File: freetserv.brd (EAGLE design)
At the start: 91.4 x 82.5 mm, 71 parts, among them IC2 SN75240PW, Q1 12MHz, Q2 6MHz, U1 MCP16311-E/MS

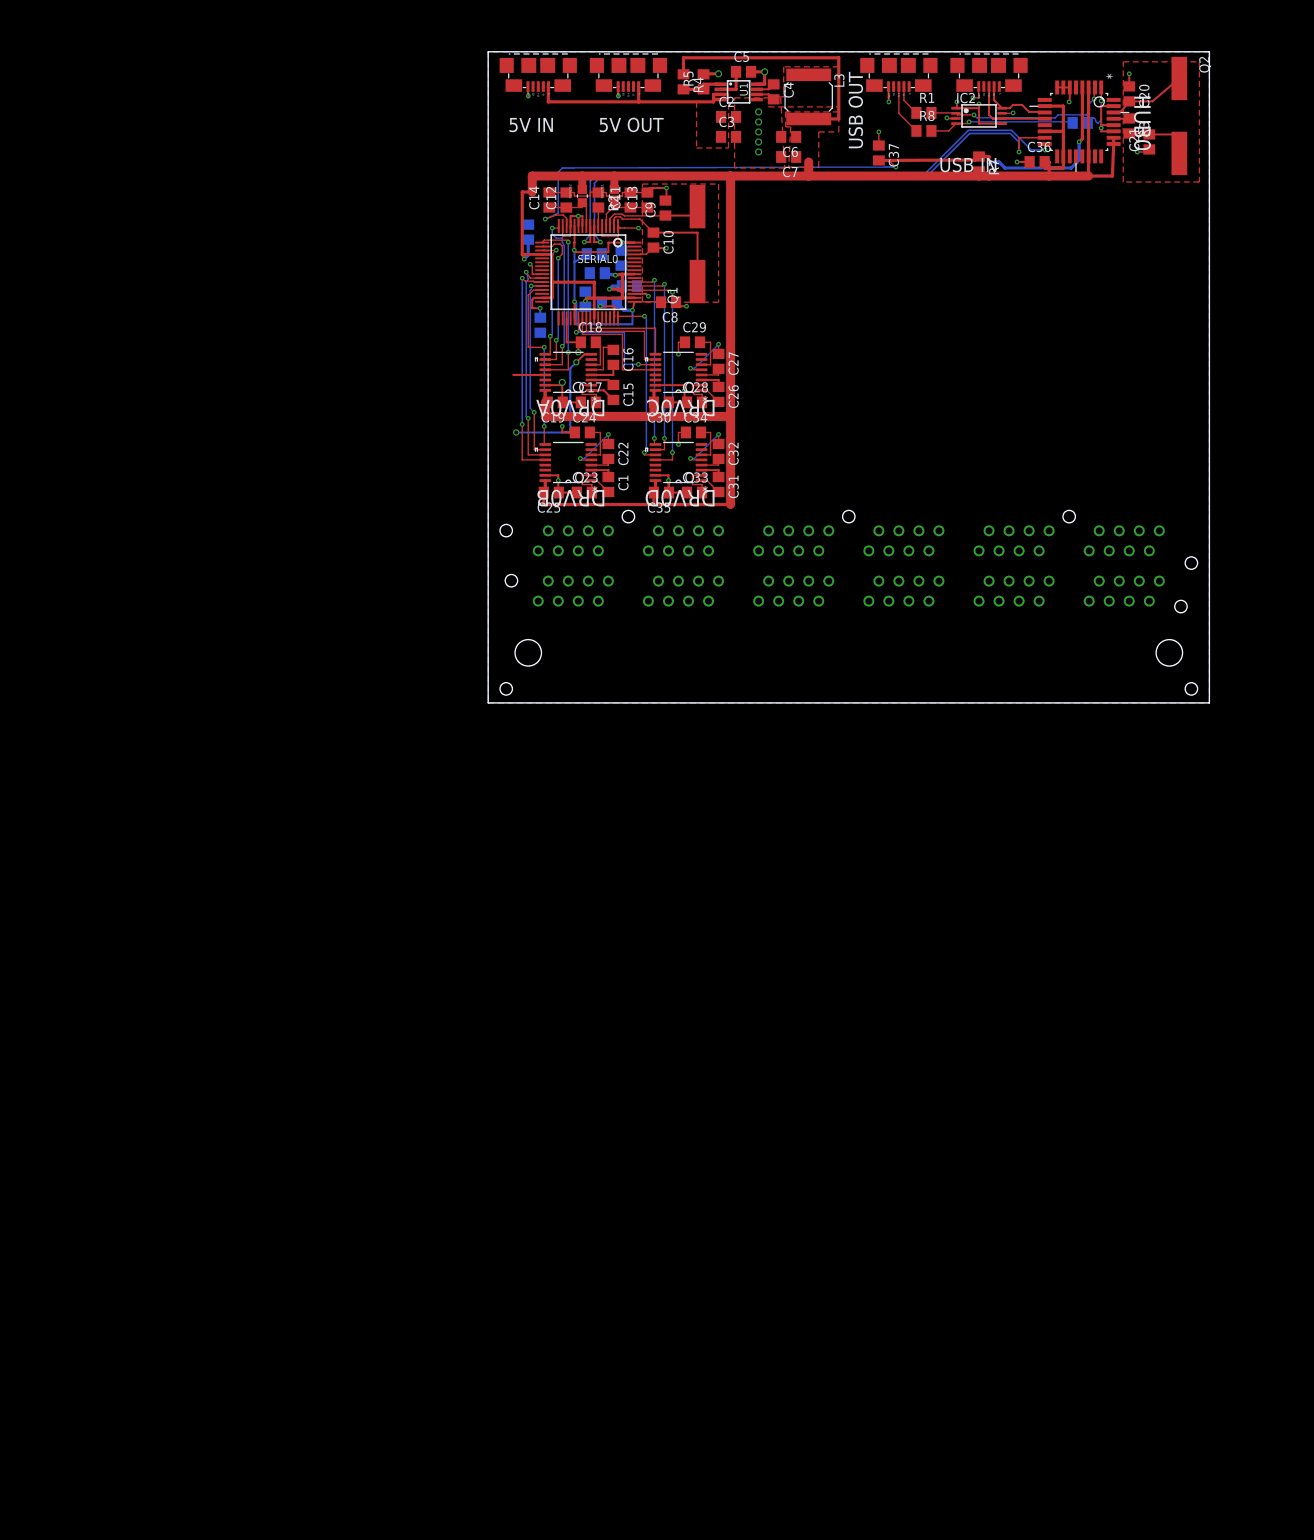
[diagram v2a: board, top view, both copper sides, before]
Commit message: Volker re-organized the schematics
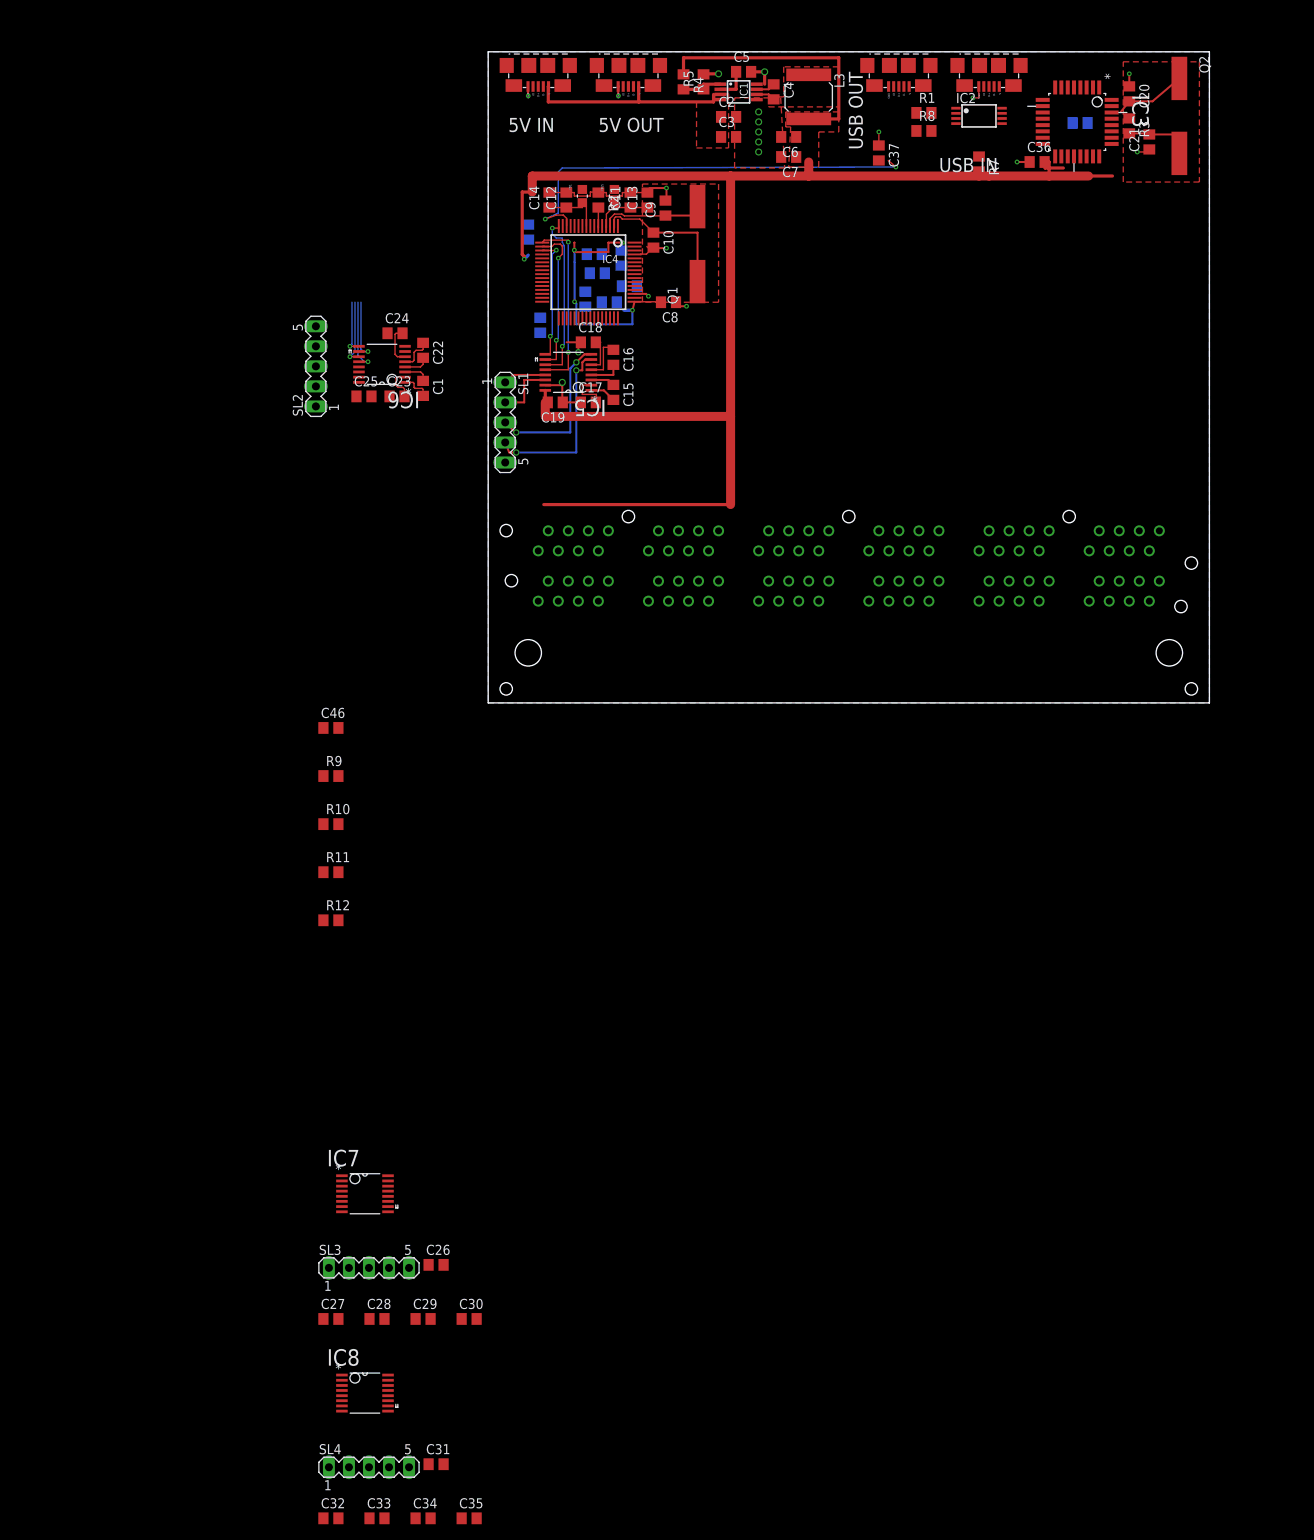
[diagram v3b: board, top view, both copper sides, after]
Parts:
- removed DRV0B, DRV0C, DRV0D: MAX3232ECPW, Texas Instruments_By_element14_Batch_1:SOP65P640X120-16N
- removed HUB0: TUSB2046BVF, Texas Instruments_By_element14_Batch_1:QFP80P900X900X145-32N
- added C46: 0.1uF, resistor:C0805
- added IC3: TUSB2046BVF, Texas Instruments_By_element14_Batch_1:QFP80P900X900X145-32N
- added IC6, IC7, IC8: MAX3232ECPW, Texas Instruments_By_element14_Batch_1:SOP65P640X120-16N
- added R10, R9: 27, resistor:R0805
- added R11, R12: 10k, resistor:R0805
- added SL1, SL2, SL3, SL4: (no value), con-lstb:MA05-1
- R2: value 12K -> 12K / 1%
- moved C32 143.9 mm to (-19.9, -103.4), turned to 0 degrees
- moved C34 141.9 mm to (-8.26, -103.4)
- moved C33 136.1 mm to (-14.1, -103.4)
- moved C35 132.3 mm to (-2.41, -103.4), turned to 0 degrees
- moved C27 131.0 mm to (-19.9, -78.1), turned to 0 degrees
- moved C31 129.3 mm to (-6.60, -96.5), turned to 0 degrees
- moved C29 128.5 mm to (-8.26, -78.1)
- moved C28 123.0 mm to (-14.1, -78.1)
- moved C30 118.7 mm to (-2.41, -78.1), turned to 0 degrees
- moved C26 116.0 mm to (-6.60, -71.2), turned to 0 degrees
- moved C24 26.9 mm to (-11.8, 46.9)
- moved C22 26.8 mm to (-8.26, 44.7)
- moved C23 26.7 mm to (-11.6, 38.9)
- moved C25 26.7 mm to (-15.7, 38.9), turned to 0 degrees
- moved C1 26.5 mm to (-8.26, 39.9)
- renumbered DRV0A to IC5, FERRITE1 to FB2\, FERRITE2 to FB1, SERIAL0 to IC4, U1 to IC1
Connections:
- net N$12 renamed DX0_N
- net N$13 renamed DX0_P
- net N$35 renamed TXD1I
- net N$36 renamed RXD1I
- net N$5 renamed RTS1I
- net N$7 renamed CTS1I
- removed net N$19: IC5.13
- removed net N$20: C1.1, DRV0B.3
- removed net N$23: DRV0B.11, IC4.26
- removed net N$24: DRV0B.12, IC4.27
- removed net N$26: C23.2, DRV0B.2
- removed net N$38: C24.2, DRV0B.6
- removed net N$41: IC2.4, R6.2, R8.2
- removed net N$43: C37.2, HUB0.4, IC4.14, R7.1
- removed net N$51: C26.2, DRV0C.1
- removed net N$54: C27.1, DRV0C.5
- removed net N$55: DRV0C.11, IC4.38
- removed net N$56: DRV0C.12, IC4.39
- removed net N$58: C28.2, DRV0C.2
- removed net N$59: C29.2, DRV0C.6
- removed net N$65: C31.2, DRV0D.1
- removed net N$68: C32.1, DRV0D.5
- removed net N$69: DRV0D.11, IC4.48
- removed net N$70: DRV0D.12, IC4.52
- removed net N$72: C33.2, DRV0D.2
- removed net N$73: C34.2, DRV0D.6
- removed net N$75: DRV0D.10, IC4.53
- removed net N$76: DRV0D.9, IC4.54
- removed net N$9: IC5.8
- removed net USB0_D2_N: HUB0.15, IC4.7
- removed net USB0_D2_P: HUB0.16, IC4.8
- removed net USB0_DM_N: HUB0.2, IC2.2, R1.2
- removed net USB0_DM_P: HUB0.1, R6.1
- new net !OVRCUR1: IC3.10, R11.2
- new net !OVRCUR2: IC3.14, R12.2
- new net !OVRCUR3: IC3.18
- new net !OVRCUR4: IC3.22
- new net !PWRON1: IC3.9
- new net !PWRON2: IC3.13
- new net !PWRON3: IC3.17
- new net !PWRON4: IC3.21
- new net !RESET: C37.2, IC3.4, IC4.14, R7.1
- new net CTS1E: IC5.8, SL1.3
- new net CTS2E: IC6.8, SL2.3
- new net CTS2I: IC4.29, IC6.9
- new net CTS3E: IC7.8, SL3.3
- new net CTS3I: IC4.41, IC7.9
- new net CTS4E: IC8.8, SL4.3
- new net CTS4I: IC4.54, IC8.9
- new net D0_N: IC2.6, IC3.2, R1.2
- new net D0_P: IC2.8, IC3.1, R6.2, R8.2
- new net D1_N: IC2.4, IC3.11, R9.2
- new net D1_P: IC2.2, IC3.12, R10.2
- new net D2_N: IC3.15, IC4.7
- new net D2_P: IC3.16, IC4.8
- new net D3_N: IC3.19
- new net D3_P: IC3.20
- new net D4_N: IC3.23
- new net D4_P: IC3.24
- new net DX1_N: R9.1, USB_IN.D-
- new net DX1_P: R10.1, USB_IN.D+
- new net N$12: C22.1, IC6.5
- new net N$49: C27.1, IC7.5
- new net N$60: C31.2, IC8.1
- new net N$63: C32.1, IC8.5
- new net RTS1E: IC5.7, SL1.4
- new net RTS2E: IC6.7, SL2.4
- new net RTS2I: IC4.28, IC6.10
- new net RTS3E: IC7.7, SL3.4
- new net RTS3I: IC4.40, IC7.10
- new net RTS4E: IC8.7, SL4.4
- new net RTS4I: IC4.53, IC8.10
- new net RXD1E: IC5.13, SL1.1
- new net RXD2E: IC6.13, SL2.1
- new net RXD2I: IC4.27, IC6.12
- new net RXD3E: IC7.13, SL3.1
- new net RXD3I: IC4.39, IC7.12
- new net RXD4E: IC8.13, SL4.1
- new net RXD4I: IC4.52, IC8.12
- new net TXD1E: IC5.14, SL1.2
- new net TXD2E: IC6.14, SL2.2
- new net TXD2I: IC4.26, IC6.11
- new net TXD3E: IC7.14, SL3.2
- new net TXD3I: IC4.38, IC7.11
- new net TXD4E: IC8.14, SL4.2
- new net TXD4I: IC4.48, IC8.11
- net +3V3: now also C46.2, IC3.25, IC3.26, IC3.3, IC6.16, IC7.16, IC8.16, R11.1, R12.1, R6.1; no longer DRV0B.16, DRV0C.16, DRV0D.16, HUB0.10, HUB0.14, HUB0.18, HUB0.22, HUB0.25, HUB0.26, HUB0.3
- net GND: now also C46.1, IC3.27, IC3.28, IC3.31, IC3.7, IC3.8, IC6.15, IC7.15, IC8.15, SL1.5, SL2.5, SL3.5, SL4.5; no longer DRV0B.15, DRV0C.15, DRV0D.15, HUB0.27, HUB0.28, HUB0.31, HUB0.6, HUB0.7, HUB0.8
- net N$1: now also C1.2, IC6.1; no longer HUB0.12, IC2.6, USB_IN.D+
- net N$11: now also C22.2, IC6.4; no longer C1.2, DRV0B.1
- net N$2: now also C1.1, IC6.3; no longer HUB0.11, IC2.8, USB_IN.D-
- net N$21: now also C23.2, IC6.2; no longer C22.2, DRV0B.4
- net N$22: now also C24.2, IC6.6; no longer C22.1, DRV0B.5
- net N$37: now also IC3.29, R3.1; no longer IC5.14
- net N$44: now also IC3.30; no longer HUB0.30
- net N$46: now also C26.2, IC7.1; no longer HUB0.29, R3.1
- net N$47: now also C26.1, IC7.3; no longer DRV0B.10, IC4.28
- net N$48: now also C27.2, IC7.4; no longer DRV0B.9, IC4.29
- net N$52: now also C28.2, IC7.2; no longer C26.1, DRV0C.3
- net N$53: now also C29.2, IC7.6; no longer C27.2, DRV0C.4
- net N$61: now also C31.1, IC8.3; no longer DRV0C.10, IC4.40
- net N$62: now also C32.2, IC8.4; no longer DRV0C.9, IC4.41
- net N$66: now also C33.2, IC8.2; no longer C31.1, DRV0D.3
- net N$67: now also C34.2, IC8.6; no longer C32.2, DRV0D.4
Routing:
- net N$43: track 92.8 -> 0.00 mm, vias 4 -> 0
- net +3V3: track 306.9 -> 220.2 mm, vias 5 -> 1
- net GND: track 137.3 -> 53.9 mm, vias 37 -> 20
- net USB0_D2_N: track 74.0 -> 0.00 mm, vias 2 -> 0
- net USB0_D2_P: track 72.9 -> 0.00 mm, vias 2 -> 0
- net !RESET: track 0.00 -> 55.2 mm, vias 0 -> 2
- net N$24: track 29.4 -> 0.00 mm, vias 2 -> 0
- net N$70: track 28.8 -> 0.00 mm, vias 2 -> 0
- net N$23: track 28.2 -> 0.00 mm, vias 2 -> 0
- net N$75: track 26.3 -> 0.00 mm, vias 2 -> 0
- net N$47: track 24.1 -> 0.00 mm, vias 2 -> 0
- net USB0_DM_N: track 24.0 -> 0.00 mm, vias 2 -> 0
- net N$76: track 23.8 -> 0.00 mm, vias 2 -> 0
- net RTS1E: track 0.00 -> 23.4 mm, vias 0 -> 2
- net N$48: track 23.3 -> 0.00 mm, vias 2 -> 0
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
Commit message: Volker re-routed the FTDI (work-in-progress)
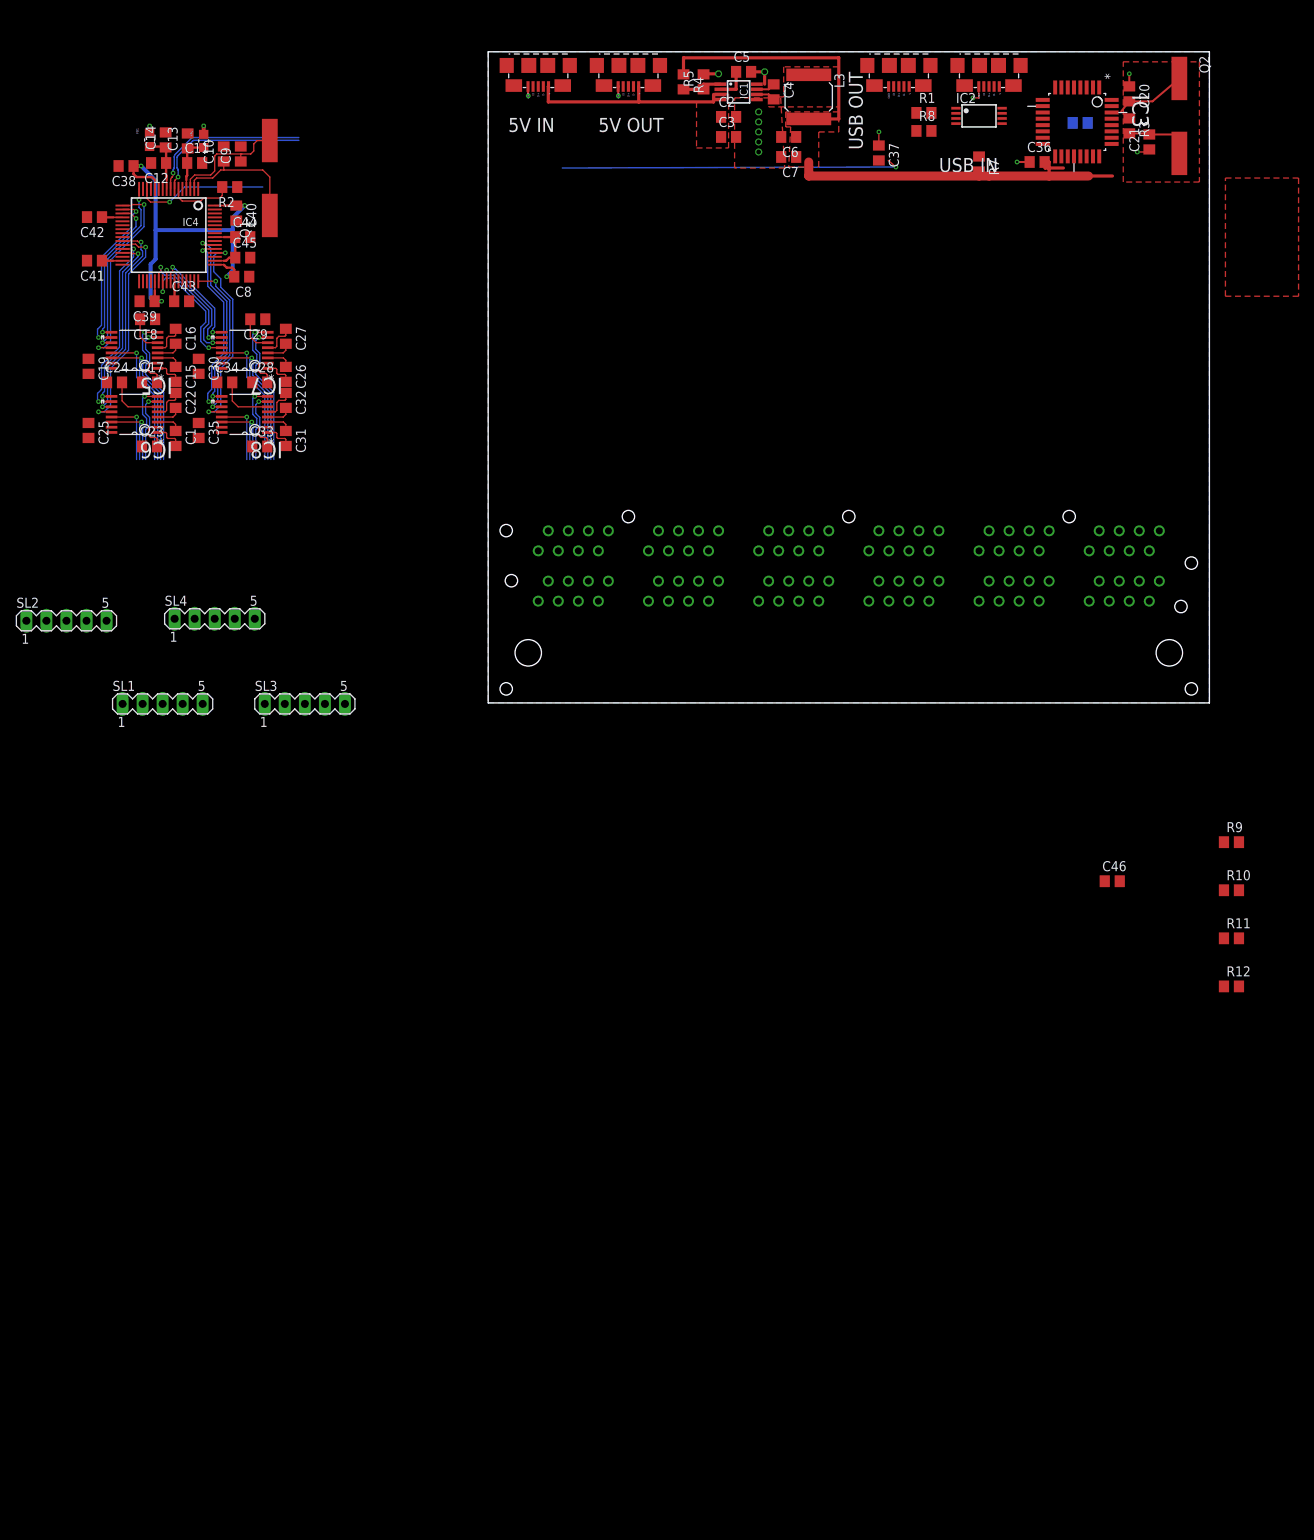
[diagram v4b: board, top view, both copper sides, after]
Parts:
- moved C34 146.2 mm to (-33.4, 40.6)
- moved C35 142.1 mm to (-36.7, 34.5), turned to 270 degrees
- moved C32 141.8 mm to (-25.7, 38.4), turned to 270 degrees
- moved C33 136.7 mm to (-29.0, 32.5)
- moved C31 131.4 mm to (-25.7, 33.5), turned to 270 degrees
- moved C29 128.5 mm to (-29.2, 48.6), turned to 180 degrees
- moved C30 125.6 mm to (-36.7, 42.7), turned to 270 degrees
- moved IC8 125.0 mm to (-30.9, 36.6), turned to 180 degrees
- moved C27 124.7 mm to (-25.7, 46.5), turned to 270 degrees
- moved C28 119.7 mm to (-29.0, 40.6)
- moved C26 114.5 mm to (-25.7, 41.7), turned to 270 degrees
- moved R10 114.5 mm to (94.2, -23.7)
- moved R11 114.5 mm to (94.2, -29.8)
- moved R12 114.5 mm to (94.2, -35.9)
- moved R9 114.5 mm to (94.2, -17.7)
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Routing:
- net +3V3: track 220.2 -> 97.7 mm, vias 1 -> 2
- net GND: track 53.9 -> 16.6 mm, vias 20 -> 14
- net RXD4I: track 0.00 -> 27.0 mm, vias 0 -> 2
- net RTS4I: track 0.00 -> 24.6 mm, vias 0 -> 2
- net CTS4I: track 0.00 -> 24.4 mm, vias 0 -> 2
- net +1V8: track 33.4 -> 57.0 mm
- net D2_P: track 0.00 -> 21.0 mm, vias 0 -> 1
- net TXD4I: track 0.00 -> 20.9 mm, vias 0 -> 2
- net D2_N: track 0.00 -> 20.6 mm, vias 0 -> 1
- net CTS3E: track 0.00 -> 19.3 mm, vias 0 -> 1
- net RXD2I: track 9.48 -> 28.6 mm, vias 1 -> 2
- net TXD2I: track 8.31 -> 26.6 mm, vias 1 -> 2
- net RTS3E: track 0.00 -> 18.1 mm, vias 0 -> 1
- net TXD3E: track 0.00 -> 17.7 mm, vias 0 -> 1
- net RXD3E: track 0.00 -> 17.6 mm, vias 0 -> 1
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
